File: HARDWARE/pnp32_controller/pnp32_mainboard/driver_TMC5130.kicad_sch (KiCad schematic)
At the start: 26 parts, among them J2 MOTOR, U8 TMC5130A-TA

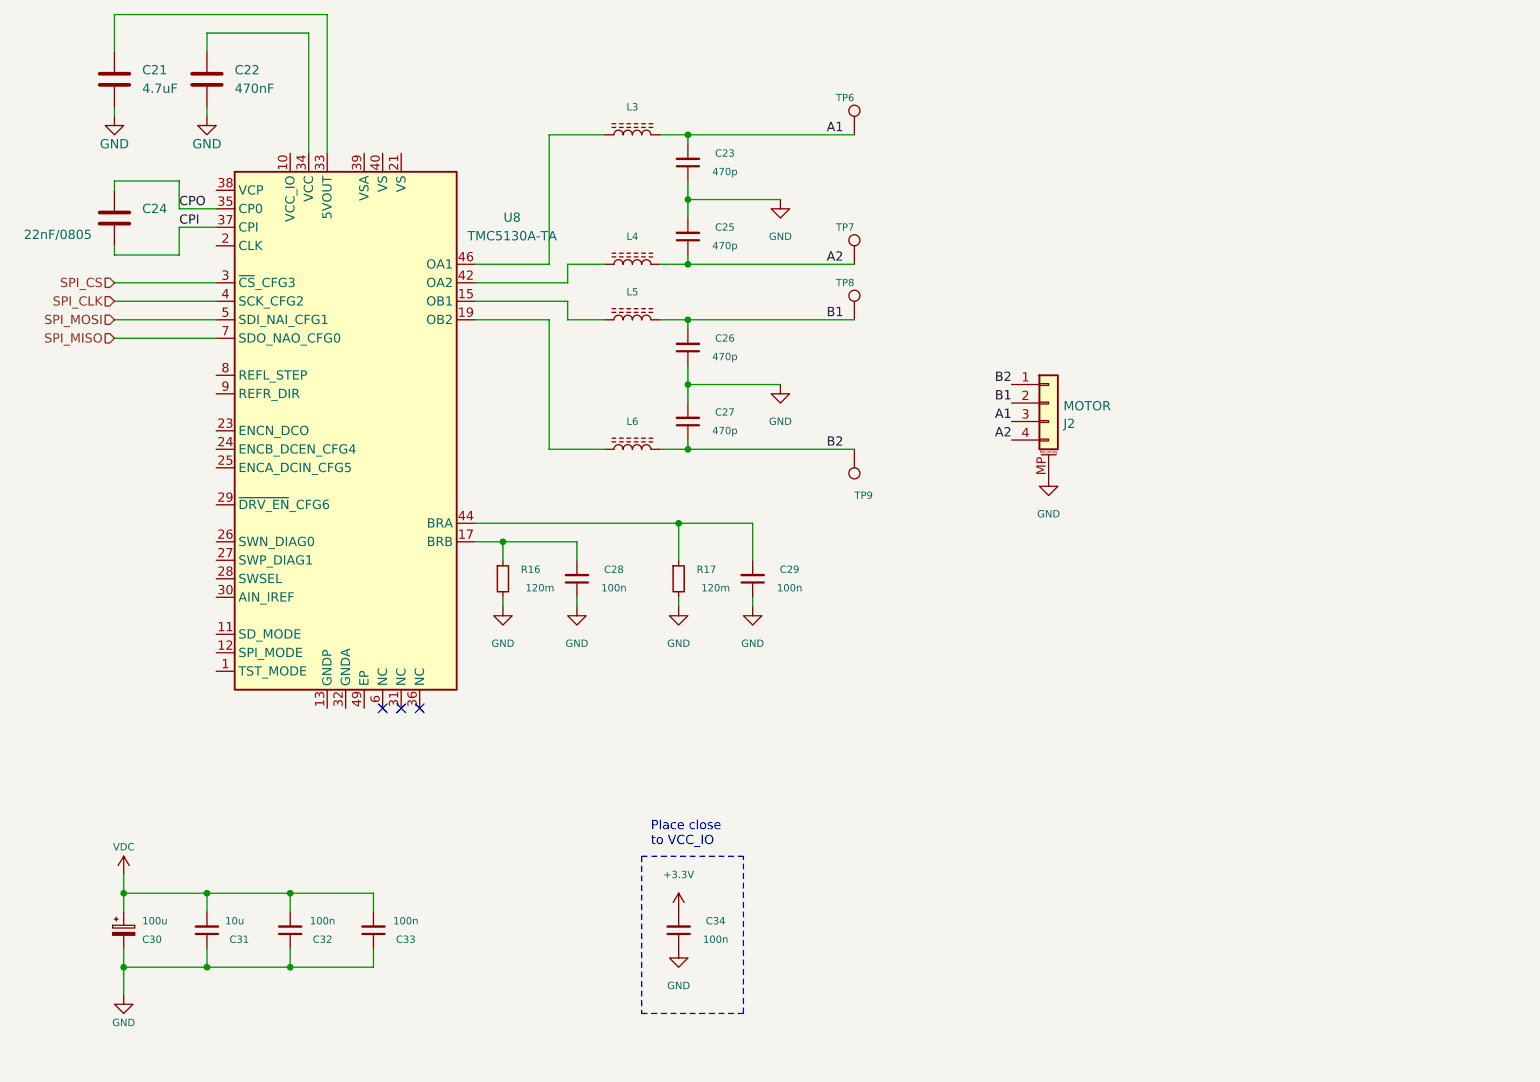
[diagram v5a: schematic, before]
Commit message: update_PSU
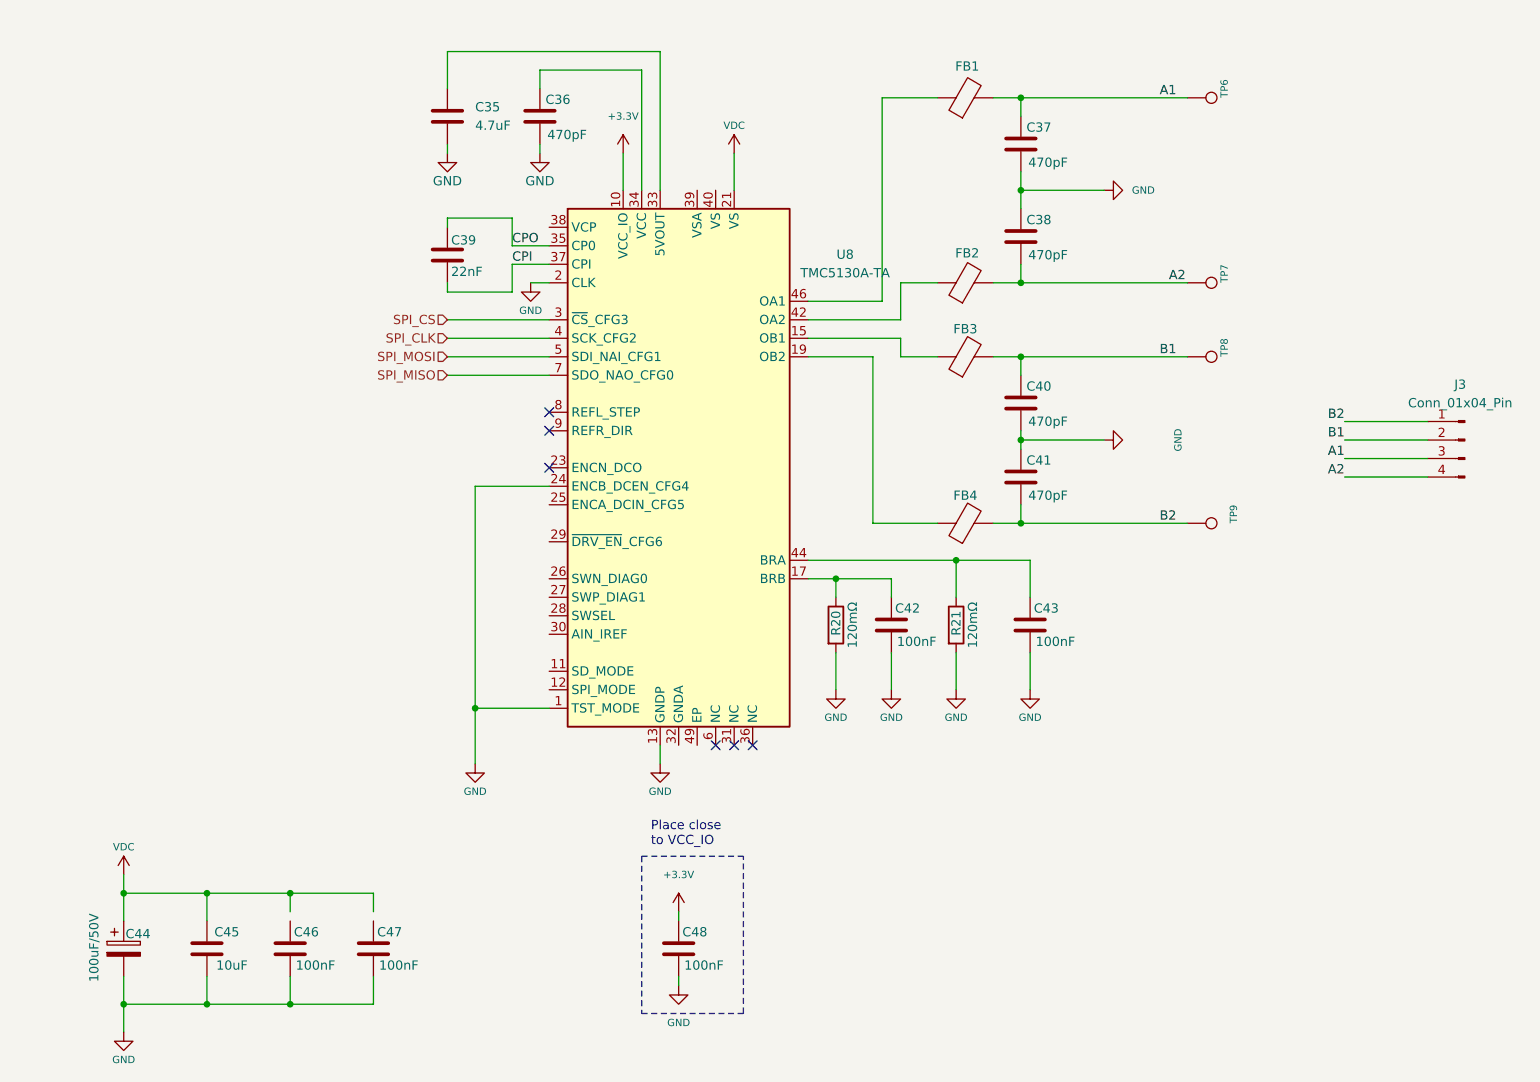
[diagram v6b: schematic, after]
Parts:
- removed C21: 4.7uF, fab_C:C_0603, symbol fab_C:C_4.7uF_0603
- removed C22: 470nF, fab_C:C_0603, symbol fab_C:C_75pF_0603
- removed C23, C25, C26, C27: 470p, Capacitor_SMD:C_0805_2012Metric, symbol Device:C_Small
- removed C24: 22nF/0805, fab_C:C_0805, symbol fab_C:C_100nF_0805
- removed C28, C29, C32, C33, C34: 100n, Capacitor_SMD:C_0805_2012Metric, symbol Device:C_Small
- removed C30: 100u, Capacitor_SMD:CP_Elec_6.3x7.7, symbol Device:C_Polarized_Small
- removed C31: 10u, Capacitor_SMD:C_0805_2012Metric, symbol Device:C_Small
- removed J2: MOTOR, Connector_JST:JST_PH_B4B-PH-SM4-TB_1x04-1MP_P2.00mm_Vertical, symbol Connector_Generic_MountingPin:Conn_01x04_MountingPin
- removed L3, L4, L5, L6: L_Ferrite, Inductor_SMD:L_0805_2012Metric, symbol Device:L_Ferrite
- removed R16, R17: 120m, Resistor_SMD:R_2512_6332Metric, symbol Device:R_Small
- added C35: 4.7uF, fab_C:C_0603, symbol fab_C:C_4.7uF_0603_16V
- added C36, C37, C38, C40, C41: 470pF, fab_C:C_0805, symbol fab_C:C_470pF_0805
- added C39: 22nF, fab_C:C_0603, symbol fab_C:C_22nF_0603
- added C42, C43, C46, C47, C48: 100nF, fab_C:C_0603, symbol fab_C:C_100nF_0603_50V
- added C44: 100uF/50V, fab_C_Pol:CP_Elec_8x10.5, symbol fab_C_Pol:C_Pol_100uF_SMD,D8xL10.5mm
- added C45: 10uF, fab_C:C_1210, symbol fab_C:C_10uF_1210_50V
- added FB1, FB2, FB3, FB4: FerriteBead, fab_R:R_0805, symbol fab_L:MPZ2012S101ATD25
- added J3: Conn_01x04_Pin, fab_CON:WE_620304124022, symbol fab_CON:WE_620304124022
- added R20, R21: 120mΩ, fab_R:R_2512, symbol fab_R:R_120mΩ_2512
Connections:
- net +3.3V: now also U8.10 (VCC_IO), C48.1
- net A1: now also C37.1, FB1.2, J3.3 (Pin_3)
- net A2: now also C38.2, FB2.2, J3.4 (Pin_4)
- net B1: now also C40.1, FB3.2, J3.2 (Pin_2)
- net B2: now also C41.2, FB4.2, J3.1 (Pin_1)
- net CPI: now also C39.2
- net CPO: now also C39.1
- net GND: now also U8.1 (TST_MODE), U8.13 (GNDP), U8.2 (CLK), U8.24 (ENCB_DCEN_CFG4), U8.48 (GNDP), C35.2, C36.2, C37.2, C38.1, C40.2, C41.1, C42.2, C43.2, C44.2, C45.2, C46.2, C47.2, C48.2, R20.2, R21.2
- net VDC: now also U8.21 (VS), C44.1, C45.1
- net at U8.44 (BRA): now also C43.1, R21.1
- net at U8.15 (OB1): now also FB3.1
- net at U8.17 (BRB): now also C42.1, R20.1
- net at U8.19 (OB2): now also FB4.1
- net at U8.33 (5VOUT): now also C35.1
- net at U8.34 (VCC): now also C36.1
- net at U8.42 (OA2): now also FB2.1
- net at U8.46 (OA1): now also FB1.1
- no-connect marks 3 -> 6
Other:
- moved on the sheet: TP6, TP7, TP8, TP9, U8
